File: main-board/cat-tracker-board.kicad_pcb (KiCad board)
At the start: 2 copper layers, 69.5 x 29 mm, 41 parts, among them J1 Conn_01x10, J2 USB_C_Receptacle_USB2.0, J3 Conn_01x03, J4 Conn_01x02, Q1 SI3443DDV-T1-GE3, Q2 Q_PNP_BCE, Q3 Q_NPN_BCE, Q4 SI3443DDV-T1-GE3, Q5 SI3443DDV-T1-GE3, U1 ATSAMD21E18A-A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

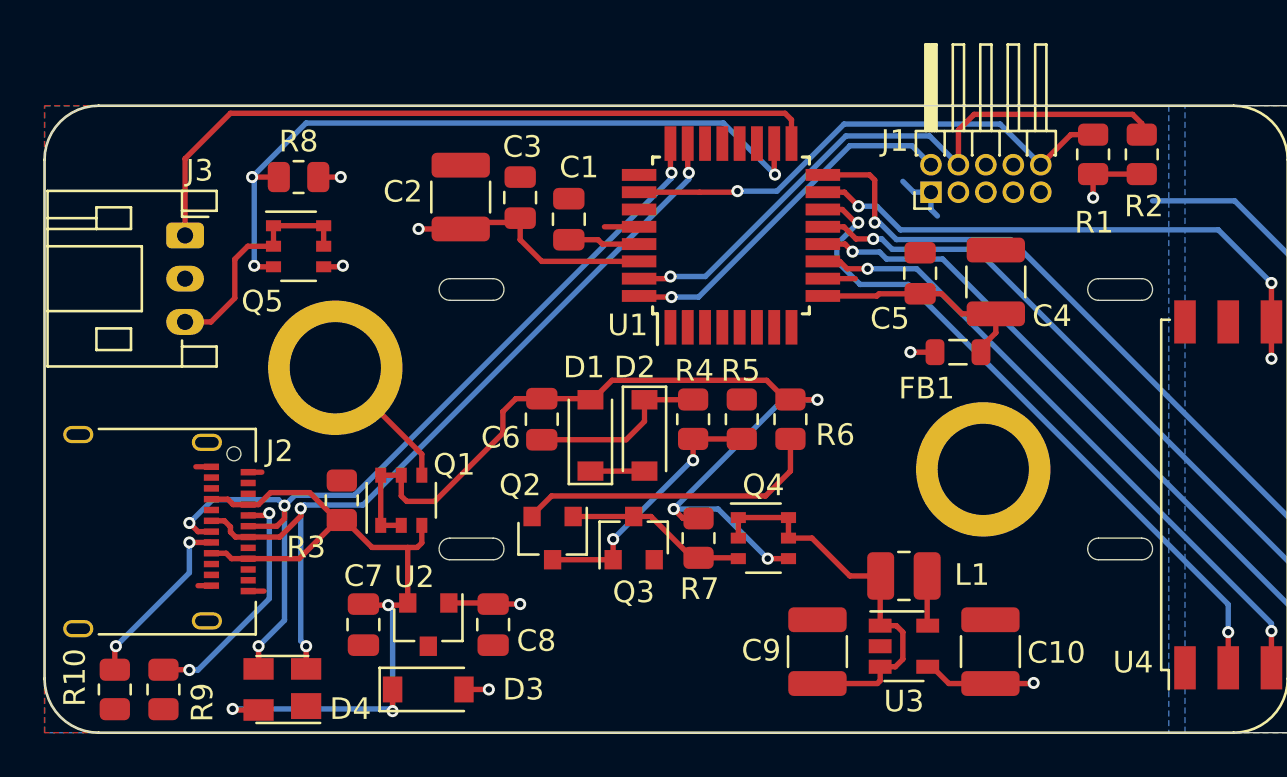
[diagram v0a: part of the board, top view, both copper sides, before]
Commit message: Added version number to boards.
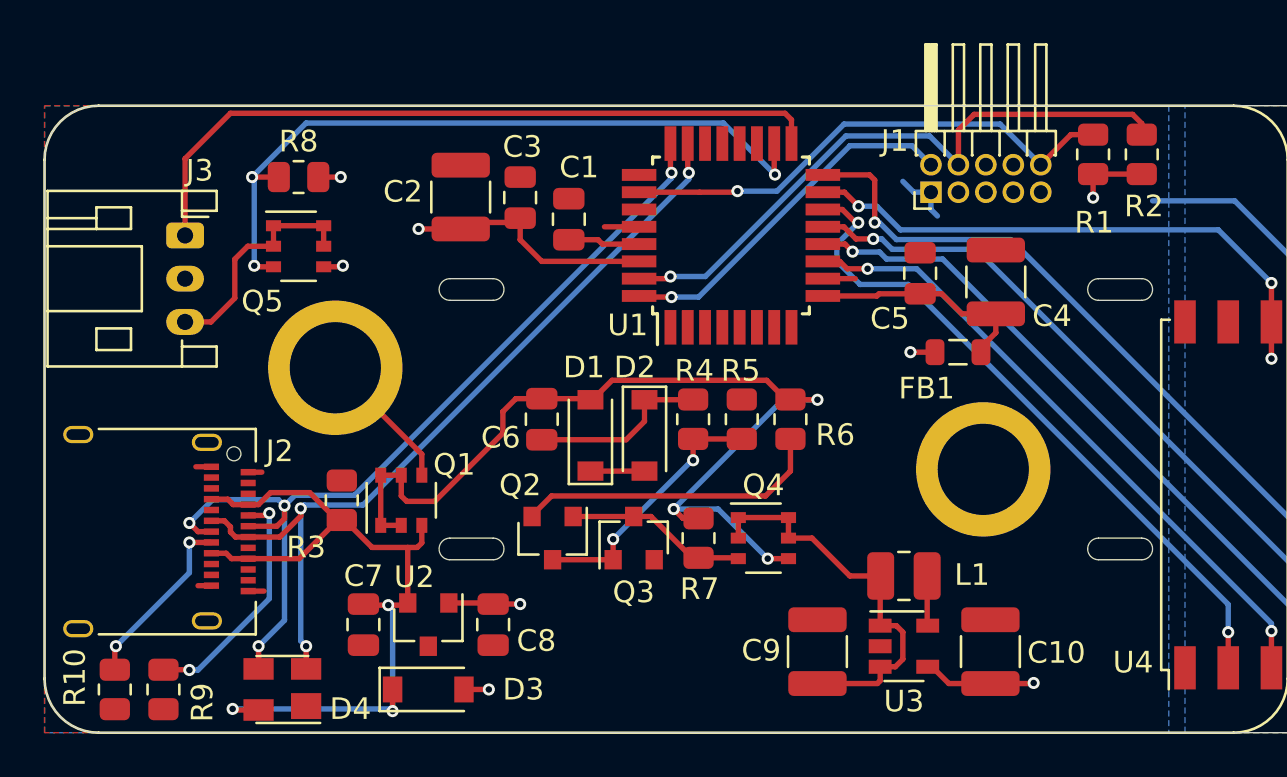
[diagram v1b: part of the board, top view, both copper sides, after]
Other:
- board text added: "v0.0.0"

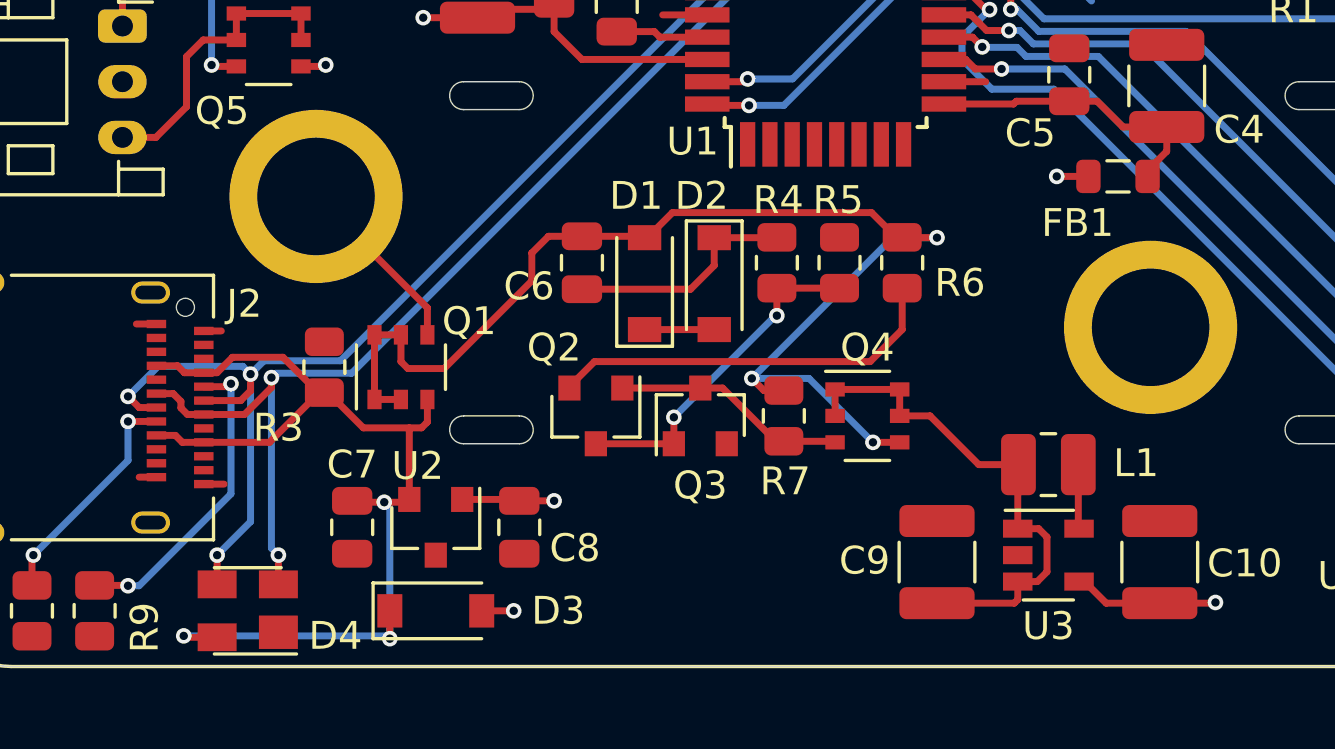
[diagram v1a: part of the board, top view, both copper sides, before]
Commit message: Remove LVP circuit and usb/bat selector switch, add slide switch for bat, change switch ind to 10uH.
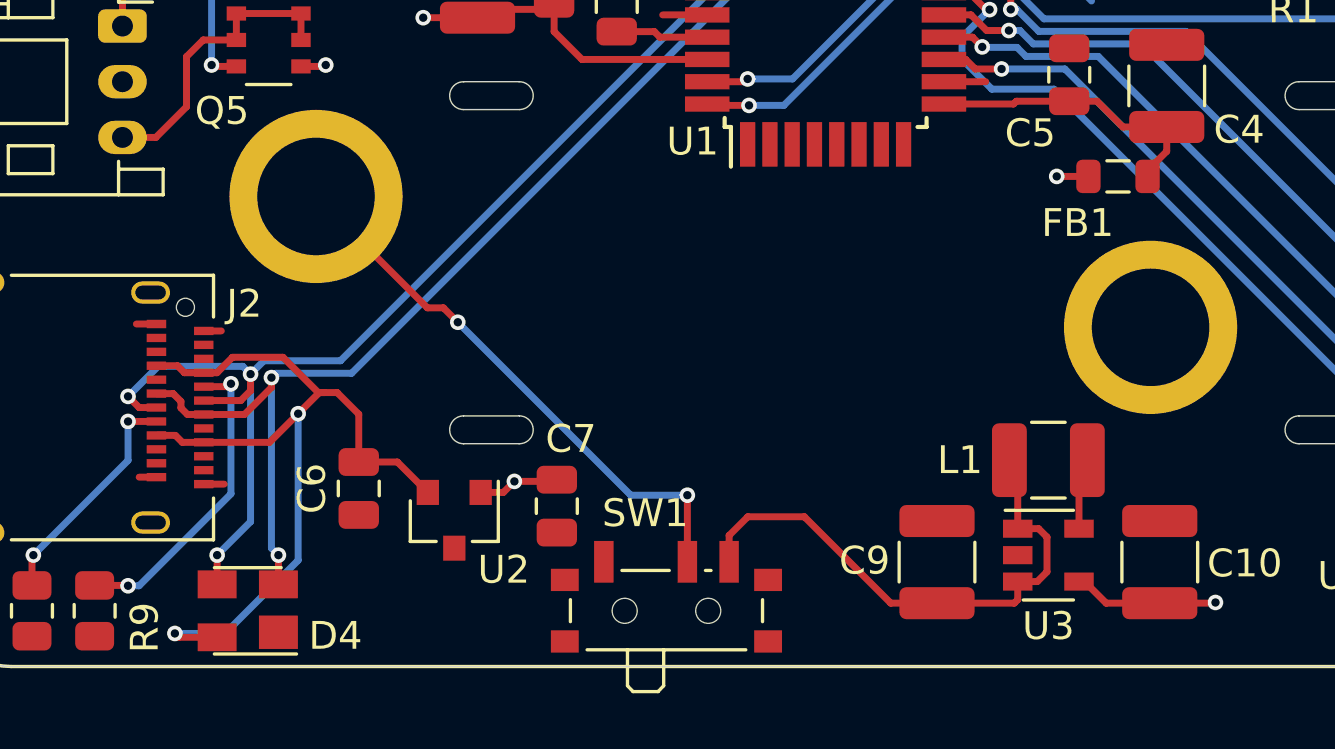
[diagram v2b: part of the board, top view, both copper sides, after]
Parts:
- removed C8: 0.1 uF, Capacitor_SMD:C_0805_2012Metric
- removed D1, D2: D, Diode_SMD:D_SOD-123
- removed D3: D_Schottky, Diode_SMD:D_SOD-123
- removed G***: LOGO, colinholzman:CPH-0.25x0.4-F.Mask
- removed Q1, Q4: SI3443DDV-T1-GE3, Package_SO:TSOP-6_1.65x3.05mm_P0.95mm
- removed Q2: Q_PNP_BCE, Package_TO_SOT_SMD:SOT-23
- removed Q3: Q_NPN_BCE, Package_TO_SOT_SMD:SOT-23
- removed R3, R5: 100k, Resistor_SMD:R_0805_2012Metric
- removed R4: 270k, Resistor_SMD:R_0805_2012Metric
- removed R6, R7: 510k, Resistor_SMD:R_0805_2012Metric
- added SW1: PCM12SMTR, Button_Switch_SMD:SW_SPDT_PCM12, F.Cu at (26.0, 26.7)
- L1: value 4.7 uH -> 10 uH; footprint Inductor_SMD:L_1008_2520Metric -> Inductor_SMD:L_1210_3225Metric
- moved C6 11.4 mm to (15.0, 22.6)
- moved C7 7.39 mm to (22.1, 23.2)
- moved U2 0.71 mm to (18.4, 23.7)
- moved L1 0.16 mm to (39.8, 21.6)
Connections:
- C6 pad 1: Net-(C6-Pad1) -> /GND
- C6 pad 2: /VBAT_SW -> /VUSB
- C7 pad 2: /VUSB -> /+3V3
- C9 pad 2: /VBAT_LVP -> /VBAT_SW
- L1 pad 2: /VBAT_LVP -> /VBAT_SW
- U3 pad 1: /VBAT_LVP -> /VBAT_SW
- U3 pad 3: /VBAT_LVP -> /VBAT_SW
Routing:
- net /VBAT_SW: track 44.2 -> 19.8 mm, vias 3 -> 0
- net /VBAT_LVP: track 18.7 -> 0.00 mm
- net Net-(Q2-Pad2): track 14.3 -> 0.00 mm
- net /VBAT: track 6.63 -> 20.2 mm, vias 0 -> 2
- net Net-(Q2-Pad3): track 12.2 -> 0.00 mm, vias 2 -> 0
- net Net-(Q2-Pad1): track 8.45 -> 0.00 mm
- net Net-(C6-Pad1): track 8.36 -> 0.00 mm
- net /VUSB: track 38.2 -> 32.3 mm, vias 3 -> 2
- net Net-(D1-Pad1): track 2.50 -> 0.00 mm
- net /+3V3: track 41.6 -> 40.1 mm, vias 9 -> 8
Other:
- board text added: "OFF"
- board text added: "ON"

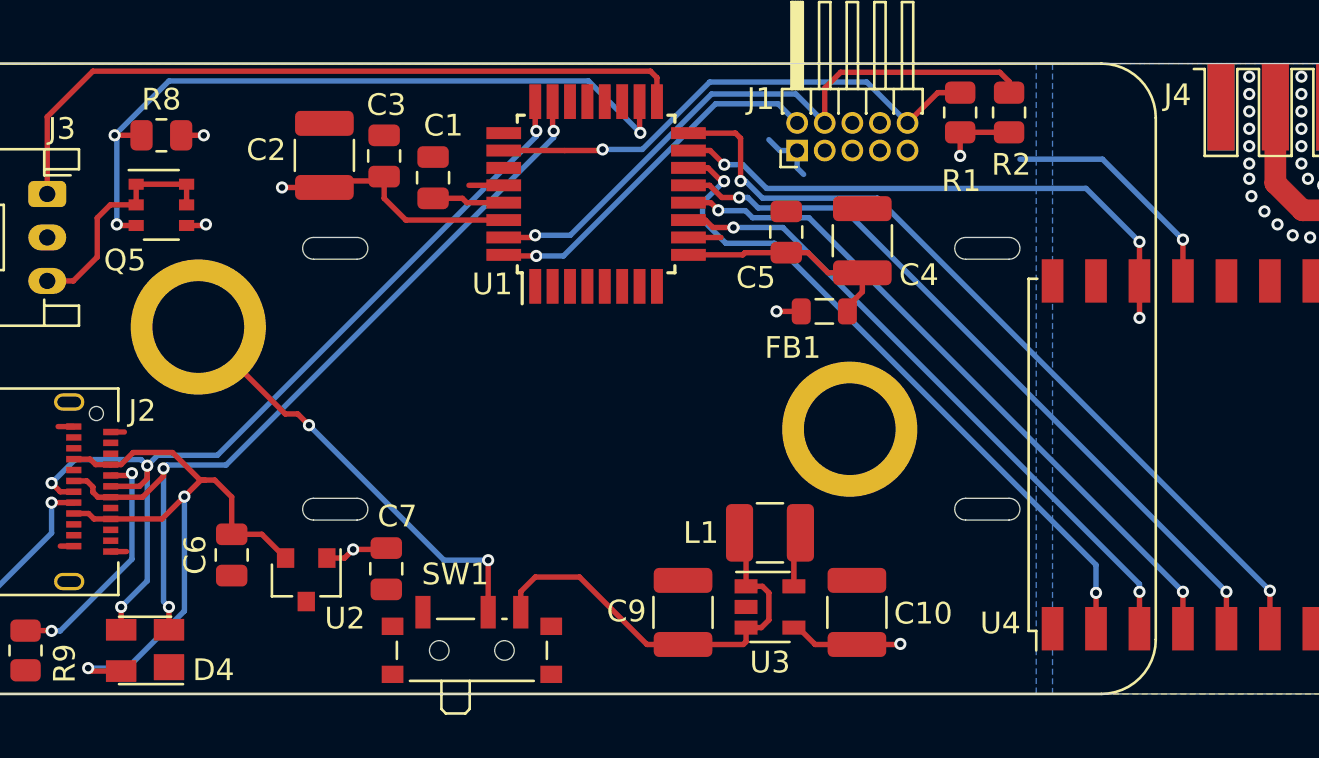
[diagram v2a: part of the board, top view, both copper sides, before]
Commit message: Improve boost converter layout, change version to 0.1.0.
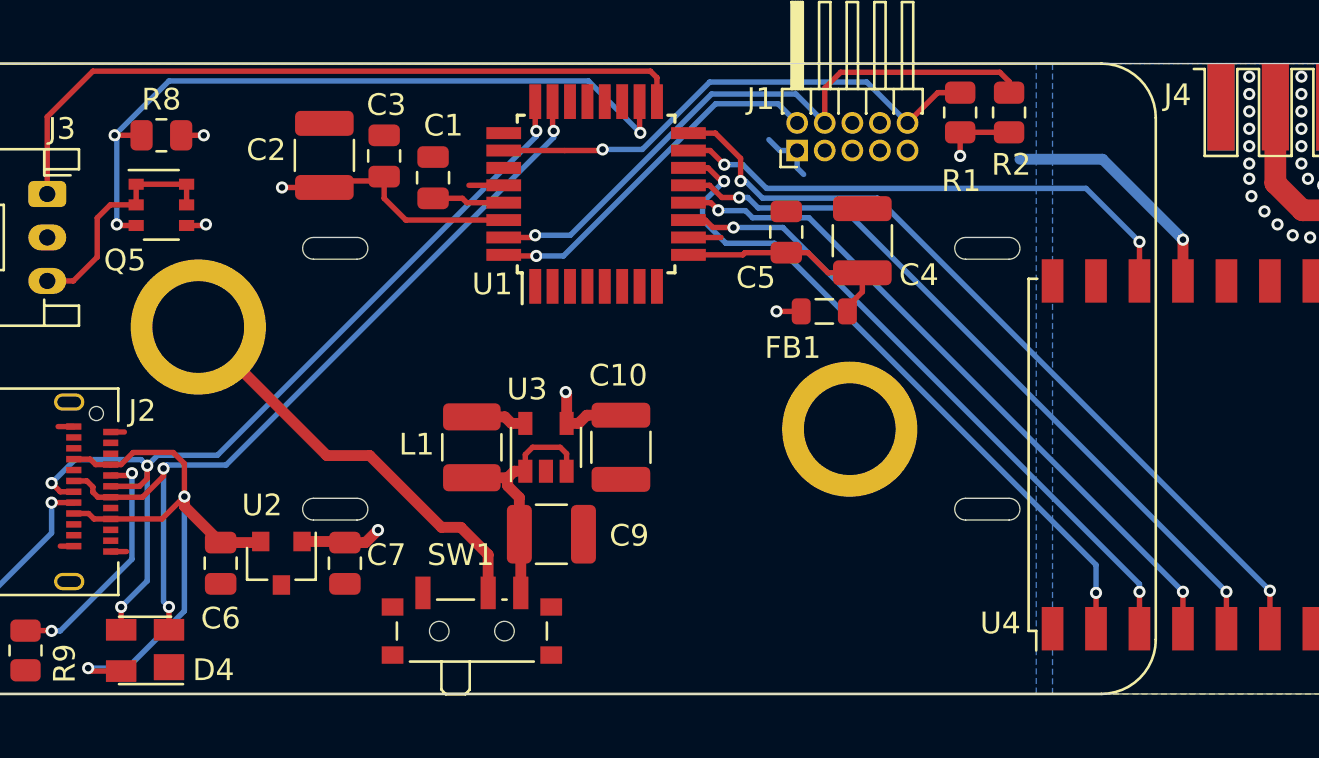
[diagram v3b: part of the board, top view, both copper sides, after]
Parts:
- added G***: LOGO, colinholzman:CPH-0.25x0.4-F.Mask, B.Cu at (63.5, 15.7)
- moved L1 14.3 mm to (26.0, 17.7), turned to 270 degrees
- moved C10 13.3 mm to (32.9, 17.7), turned to 90 degrees
- moved U3 12.7 mm to (29.4, 17.7), turned to 90 degrees
- moved C9 7.04 mm to (29.7, 21.7), turned to 180 degrees
- moved C7 1.92 mm to (20.2, 23.0)
- moved U2 1.37 mm to (17.3, 23.0)
- moved SW1 0.89 mm to (26.0, 25.8)
- moved C6 0.63 mm to (14.5, 23.0)
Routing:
- net /VBAT_SW: track 19.8 -> 11.9 mm
- net /VUSB: track 32.3 -> 29.8 mm
- net /RFM_INT: track 26.0 -> 24.3 mm, vias 3 -> 2
- net /VBAT: track 20.2 -> 19.4 mm, vias 2 -> 0
- net /RFM_RESET: track 38.4 -> 37.8 mm
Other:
- board text added: "v0.1.0"
- board text removed: "v0.0.0"

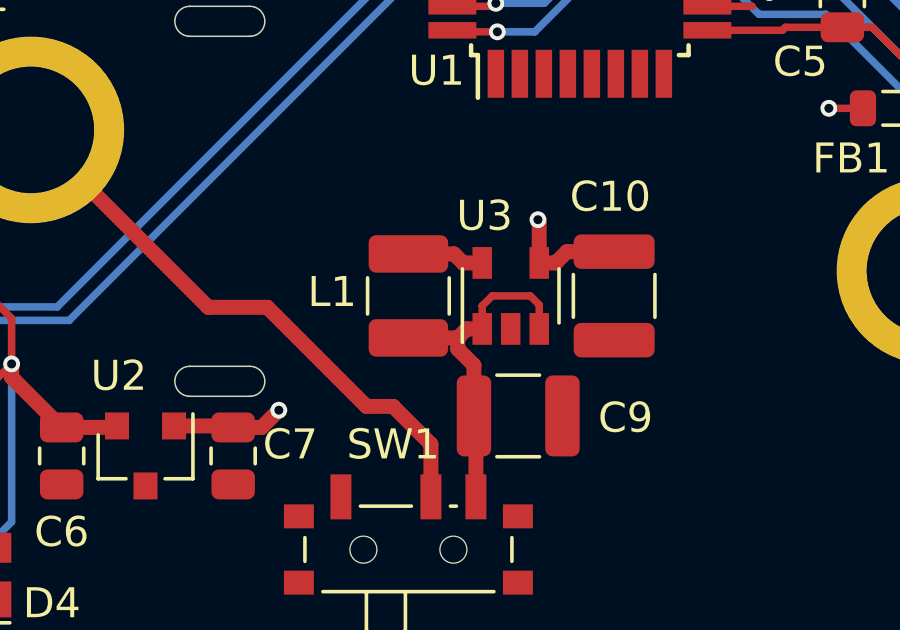
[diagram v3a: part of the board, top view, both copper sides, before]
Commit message: Change boost converter inductor to the one used in the reference design.
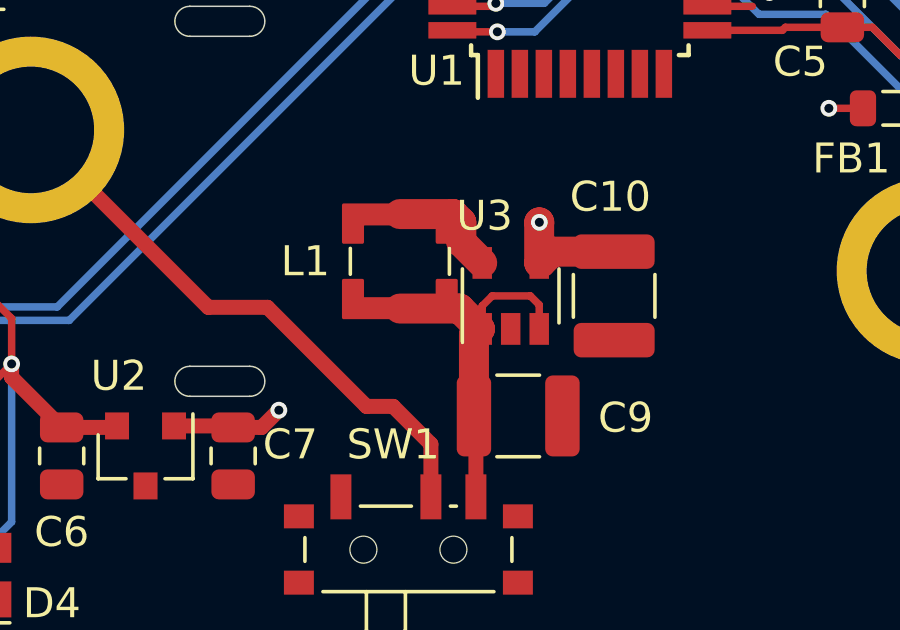
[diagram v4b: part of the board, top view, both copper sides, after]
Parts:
- L1: footprint Inductor_SMD:L_1210_3225Metric -> colinholzman:DO3314-...MLC
- moved L1 1.19 mm to (25.8, 16.5)
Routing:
- net Net-(L1-Pad1): track 2.58 -> 3.81 mm
- net /VBAT_SW: track 11.9 -> 12.4 mm

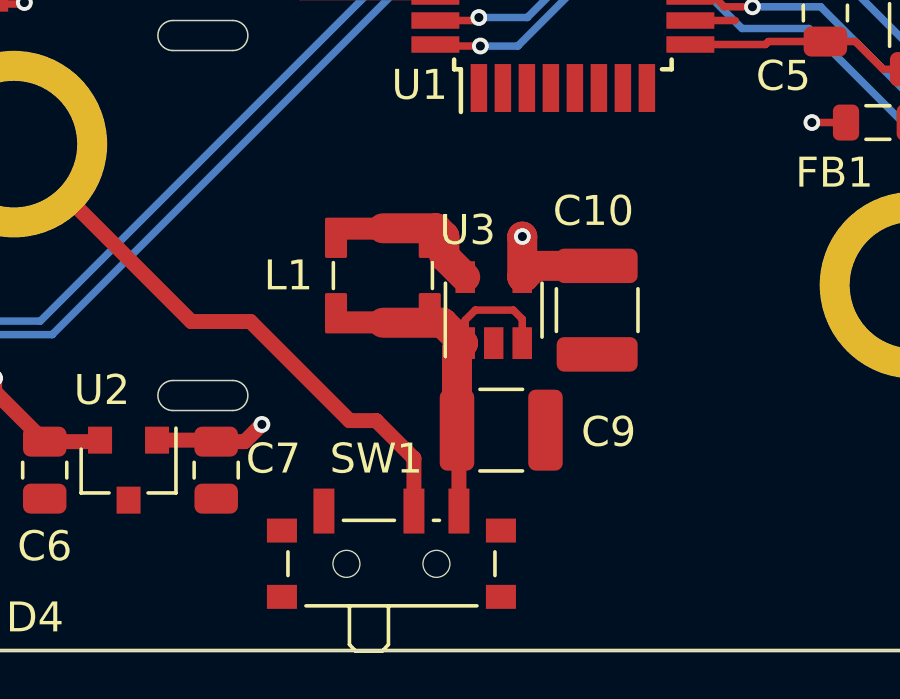
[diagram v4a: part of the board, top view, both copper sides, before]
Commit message: Remove boost converter, replace with low Vf schottky.
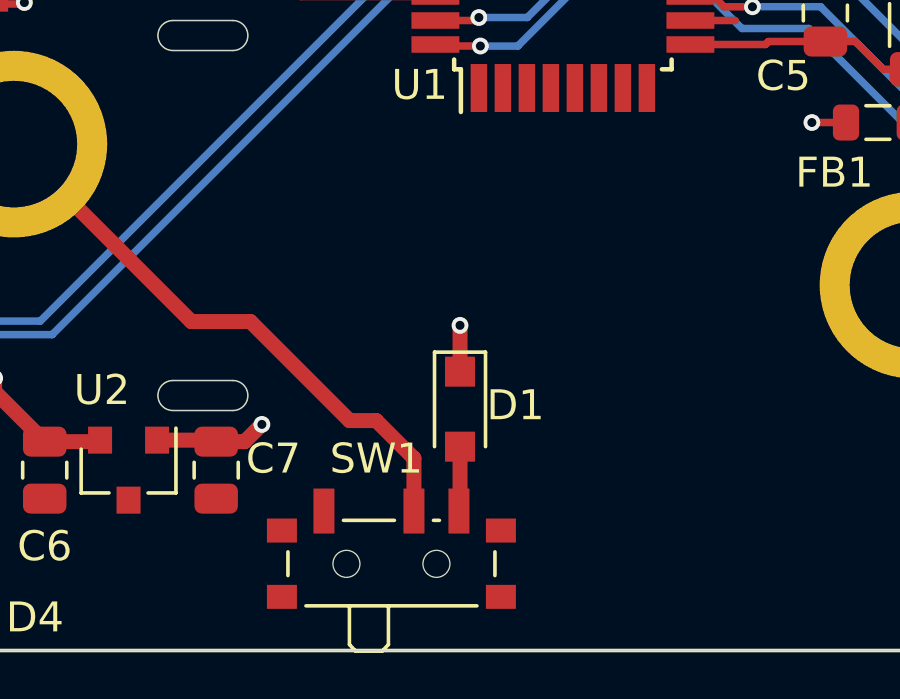
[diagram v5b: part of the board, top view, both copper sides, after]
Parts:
- removed C10, C9: 10 uF, Capacitor_SMD:C_1210_3225Metric
- removed L1: 10 uH, colinholzman:DO3314-...MLC
- removed U3: TPS61097A-33DBVR, Package_TO_SOT_SMD:SOT-23-5
- added D1: CUS08F30, Diode_SMD:D_SOD-323_HandSoldering, F.Cu at (28.3, 21.0)
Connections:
- SW1 pad 3: /VBAT_SW -> Net-(D1-Pad2)
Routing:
- net /VBAT_SW: track 12.4 -> 0.00 mm
- net Net-(L1-Pad1): track 3.81 -> 0.00 mm
- net /+3V3: track 39.7 -> 37.2 mm
- net Net-(D1-Pad2): track 0.00 -> 2.16 mm
